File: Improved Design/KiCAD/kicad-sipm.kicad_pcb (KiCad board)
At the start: 2 copper layers, 25.3 x 25.3 mm, 26 parts, among them J1 Conn_01x05, J2 Conn_Coaxial, U1 OPA847, U2 OPA842

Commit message: Commit Gerbers and fix some labeling mistakes
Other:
- board text added: "+5v"
- board text added: "-5v"
- board text added: "Designed by: Michael Giacomelli"
- board text removed: "+5"
- board text removed: "-5"
- board text removed: "Bias"
- board text removed: "Bias Voltage"
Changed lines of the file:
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@@
   (general
     (thickness 1.6)
-    (drawings 11)
+    (drawings 10)
     (tracks 133)
     (modules 26)
@@
   (module "footprints:DF13C-5P-1.25V21" (layer "F.Cu")
     (at 105.725 97.675 90)
-    (fp_text reference "J1" (at 2.65 1.05 180) (layer "F.SilkS")
+    (fp_text reference "J1" (at 2.45 1.125 180) (layer "F.SilkS")
       (effects (font (size 0.6 0.6) (thickness 0.15)))
     )
@@
     )
   )
-  (gr_text "+5" (at 108.675 102.575) (layer "F.SilkS")
+  (gr_text "Designed by:\nMichael Giacomelli" (at 99.725 110.475) (layer "B.SilkS")
+    (effects (font (size 0.6 0.6) (thickness 0.15)) (justify mirror))
+  )
+  (gr_text "+5v" (at 110.075 102.7) (layer "F.SilkS")
     (effects (font (size 0.6 0.6) (thickness 0.15)))
   )
-  (gr_text "-5" (at 108.725 100.125) (layer "F.SilkS")
+  (gr_text "GND" (at 110.2 101.4) (layer "F.SilkS")
     (effects (font (size 0.6 0.6) (thickness 0.15)))
   )
-  (gr_text "GND" (at 108.525 101.45) (layer "F.SilkS")
+  (gr_text "-5v" (at 110 99.975) (layer "F.SilkS")
     (effects (font (size 0.6 0.6) (thickness 0.15)))
   )
-  (gr_text "GND" (at 108.4 99.025) (layer "F.SilkS")
+  (gr_text "GND" (at 110.1 98.8) (layer "F.SilkS")
     (effects (font (size 0.6 0.6) (thickness 0.15)))
   )
-  (gr_text "Bias" (at 108.525 97.775) (layer "F.SilkS")
+  (gr_text "HV" (at 110.15 97.625) (layer "F.SilkS")
     (effects (font (size 0.6 0.6) (thickness 0.15)))
   )
-  (gr_text "Bias Voltage" (at 109.275 97.675) (layer "F.Cu")
-    (effects (font (size 0.6 0.6) (thickness 0.15)))
-  )
-  (gr_text "HV" (at 108.675 97.825) (layer "F.Cu")
-    (effects (font (size 0.6 0.6) (thickness 0.15)))
-  )

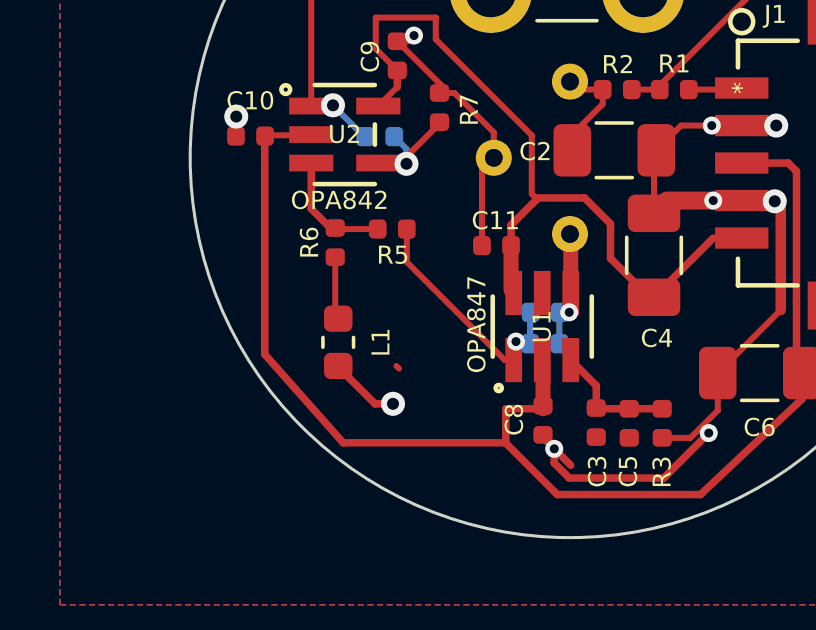
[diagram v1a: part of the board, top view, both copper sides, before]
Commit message: Update labels one more time.
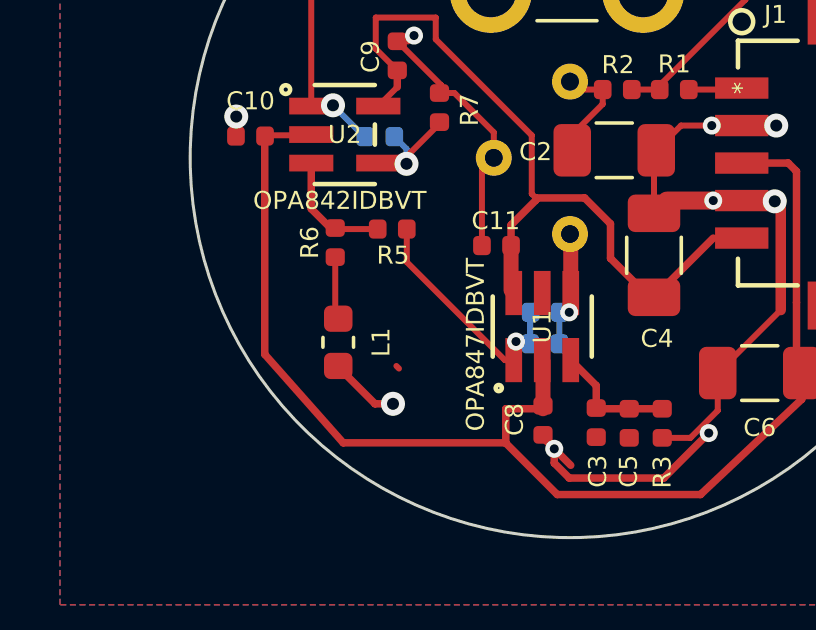
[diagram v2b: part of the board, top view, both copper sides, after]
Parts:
- J1: value Conn_01x05 -> DF13C-5P-1.25V(21)
- U1: value OPA847 -> OPA847IDBVT
- U2: value OPA842 -> OPA842IDBVT
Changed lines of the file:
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@@
       (effects (font (size 0.6 0.6) (thickness 0.15)))
     )
-    (fp_text value "OPA842" (at -0.1676 2.2) (layer "F.SilkS")
+    (fp_text value "OPA842IDBVT" (at -0.1676 2.2) (layer "F.SilkS")
       (effects (font (size 0.6 0.6) (thickness 0.15)))
     )
@@
       (effects (font (size 0.6 0.6) (thickness 0.15)))
     )
-    (fp_text value "OPA847" (at 0.075 -2.175 90) (layer "F.SilkS")
+    (fp_text value "OPA847IDBVT" (at -0.6 -2.225 90) (layer "F.SilkS")
       (effects (font (size 0.6 0.6) (thickness 0.15)))
     )
@@
       (effects (font (size 0.6 0.6) (thickness 0.15)))
     )
-    (fp_text value "Conn_01x05" (at -2.5 0 90) (layer "F.SilkS") hide
-      (effects (font (size 0.6 0.6) (thickness 0.15)))
-    )
+    (fp_text value "DF13C-5P-1.25V(21)" (at -2.5 0 90) (layer "F.SilkS") hide
+      (effects (font (size 0.6 0.6) (thickness 0.15)))
+    )
